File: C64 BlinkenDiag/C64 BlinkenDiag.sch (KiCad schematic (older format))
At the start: 14 parts, among them J1 C64-Exp-Port, J2 Voltmeter, M1 Mounting, M2 Mounting, M3 Mounting, M4 Mounting, SW1 ROM_EN, SW2 Function, SW3 Bank, SW4 Reset, U1 28C256

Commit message: Did a layout
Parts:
- added C1, C2, C3, C4, C5: 100nF, Capacitor_THT:C_Disc_D4.7mm_W2.5mm_P5.00mm, symbol Device:C_Small
- added C6: 10uF, Capacitor_THT:CP_Radial_D4.0mm_P2.00mm, symbol Device:CP_Small
- added D1: RESET, LED_THT:LED_D5.0mm, symbol Device:LED_Small
- added D10: D6, LED_THT:LED_D5.0mm, symbol Device:LED_Small
- added D11: D5, LED_THT:LED_D5.0mm, symbol Device:LED_Small
- added D12: D4, LED_THT:LED_D5.0mm, symbol Device:LED_Small
- added D13: D3, LED_THT:LED_D5.0mm, symbol Device:LED_Small
- added D14: D2, LED_THT:LED_D5.0mm, symbol Device:LED_Small
- added D15: D1, LED_THT:LED_D5.0mm, symbol Device:LED_Small
- added D16: D0, LED_THT:LED_D5.0mm, symbol Device:LED_Small
- added D17: A15, LED_THT:LED_D5.0mm, symbol Device:LED_Small
- added D18: A14, LED_THT:LED_D5.0mm, symbol Device:LED_Small
- added D19: A13, LED_THT:LED_D5.0mm, symbol Device:LED_Small
- added D2: GAME, LED_THT:LED_D5.0mm, symbol Device:LED_Small
- added D20: A12, LED_THT:LED_D5.0mm, symbol Device:LED_Small
- added D21: A11, LED_THT:LED_D5.0mm, symbol Device:LED_Small
- added D22: A10, LED_THT:LED_D5.0mm, symbol Device:LED_Small
- added D23: A9, LED_THT:LED_D5.0mm, symbol Device:LED_Small
- added D24: A8, LED_THT:LED_D5.0mm, symbol Device:LED_Small
- added D25: A7, LED_THT:LED_D5.0mm, symbol Device:LED_Small
- added D26: A6, LED_THT:LED_D5.0mm, symbol Device:LED_Small
- added D27: A5, LED_THT:LED_D5.0mm, symbol Device:LED_Small
- added D28: A4, LED_THT:LED_D5.0mm, symbol Device:LED_Small
- added D29: A3, LED_THT:LED_D5.0mm, symbol Device:LED_Small
- added D3: EXROM, LED_THT:LED_D5.0mm, symbol Device:LED_Small
- added D30: A2, LED_THT:LED_D5.0mm, symbol Device:LED_Small
- added D31: A1, LED_THT:LED_D5.0mm, symbol Device:LED_Small
- added D32: A0, LED_THT:LED_D5.0mm, symbol Device:LED_Small
- added D4: IO2, LED_THT:LED_D5.0mm, symbol Device:LED_Small
- added D5: IO1, LED_THT:LED_D5.0mm, symbol Device:LED_Small
- added D6: WRITE, LED_THT:LED_D5.0mm, symbol Device:LED_Small
- added D7: IRQ, LED_THT:LED_D5.0mm, symbol Device:LED_Small
- added D8: NMI, LED_THT:LED_D5.0mm, symbol Device:LED_Small
- added D9: D7, LED_THT:LED_D5.0mm, symbol Device:LED_Small
- added JP1: EN_SIGNAL, Connector_PinHeader_2.54mm:PinHeader_1x03_P2.54mm_Vertical, symbol Jumper:Jumper_3_Bridged12
- added JP2: EN_DATA, Connector_PinHeader_2.54mm:PinHeader_1x03_P2.54mm_Vertical, symbol Jumper:Jumper_3_Bridged12
- added JP3, JP4: EN_ADDR, Connector_PinHeader_2.54mm:PinHeader_1x03_P2.54mm_Vertical, symbol Jumper:Jumper_3_Bridged12
- added RN1, RN2, RN3, RN4: 330x8, Resistor_THT:R_Array_SIP9, symbol Device:R_Network08
- added U2: 74HCT540, Package_DIP:DIP-20_W7.62mm_Socket_LongPads, symbol 74xx:74LS540
- added U3, U4, U5: 74HCT573, Package_DIP:DIP-20_W7.62mm_Socket_LongPads, symbol 74xx:74LS573
- A1: footprint (none) -> voltmeter:voltage_display_036
- M1, M2, M3, M4: footprint mounting:M3 -> mounting:M3_pin
- SW2: value Function -> FUNCTION
- SW3: value Bank -> ROM_BANK
- SW4: value Reset -> RESET
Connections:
- net A0: now also U5.9 (D7)
- net A1: now also U5.8 (D6)
- net A10: now also U4.7 (D5)
- net A11: now also U4.6 (D4)
- net A12: now also U4.5 (D3)
- net A13: now also J1.J (A13), U4.4 (D2); no longer R1.2, SW1.4 (A), SW2.1 (A), U1.26 (A13)
- net A14: now also J1.H (A14), U4.3 (D1); no longer R2.2, SW3.1 (A), U1.1 (A14)
- net A2: now also U5.7 (D5)
- net A3: now also U5.6 (D4)
- net A4: now also U5.5 (D3)
- net A5: now also U5.4 (D2)
- net A6: now also U5.3 (D1)
- net A7: now also U5.2 (D0)
- net A8: now also U4.9 (D7)
- net A9: now also U4.8 (D6)
- net D0: now also U3.9 (D7)
- net D1: now also U3.8 (D6)
- net D2: now also U3.7 (D5)
- net D3: now also U3.6 (D4)
- net D4: now also U3.5 (D3)
- net D5: now also U3.4 (D2)
- net D6: now also U3.3 (D1)
- net D7: now also U3.2 (D0)
- net GND: now also C1.2, C2.2, C3.2, C4.2, C5.2, C6.2, JP1.1 (A), JP2.1 (A), JP3.1 (A), JP4.1 (A), RN1.1 (common), RN2.1 (common), RN3.1 (common), RN4.1 (common), U2.10 (GND), U3.10 (GND), U4.10 (GND), U5.10 (GND)
- net VCC: now also C1.1, C2.1, C3.1, C4.1, C5.1, C6.1, JP1.3 (B), JP2.3 (B), JP3.3 (B), JP4.3 (B), U2.20 (VCC), U3.20 (VCC), U4.20 (VCC), U5.20 (VCC)
- net ~EXROM: now also U2.4 (A2)
- net ~GAME: now also U2.3 (A1)
- net ~RESET: now also U2.2 (A0)
- net ~IO2: now reaches J1.10 (~IO2)
- net ~IO2: now also U2.5 (A3)
- net ~IRQ: now reaches J1.4 (~IRQ)
- net ~IRQ: now also U2.8 (A6)
- net R~W: now reaches J1.5 (R/~W)
- net R~W: now also U2.7 (A5)
- net ~IO1: now reaches J1.7 (~IO1)
- net ~IO1: now also U2.6 (A4)
- net ~NMI: now reaches J1.D (~NMI)
- net ~NMI: now also U2.9 (A7)
- net PHI2: now reaches J1.E (PHI2)
- net PHI2: now also U3.11 (Load), U4.11 (Load), U5.11 (Load)
- net A15: now reaches J1.F (A15)
- net A15: now also U4.2 (D0)
- net ~ROM renamed ~ROM_CS
- new net: JP1.2 (C), U2.1 (G1), U2.19 (G2)
- new net: D8.2 (A), U2.11 (Y7)
- new net: D7.2 (A), U2.12 (Y6)
- new net: D6.2 (A), U2.13 (Y5)
- new net: D5.2 (A), U2.14 (Y4)
- new net: D4.2 (A), U2.15 (Y3)
- new net: D3.2 (A), U2.16 (Y2)
- new net: D2.2 (A), U2.17 (Y1)
- new net: D1.2 (A), U2.18 (Y0)
- new net: D1.1 (K), RN2.2 (R1)
- new net: D2.1 (K), RN2.3 (R2)
- new net: D3.1 (K), RN2.4 (R3)
- new net: D4.1 (K), RN2.5 (R4)
- new net: D5.1 (K), RN2.6 (R5)
- new net: D6.1 (K), RN2.7 (R6)
- new net: D7.1 (K), RN2.8 (R7)
- new net: D8.1 (K), RN2.9 (R8)
- new net: JP2.2 (C), U3.1 (OE)
- new net: D16.2 (A), U3.12 (Q7)
- new net: D15.2 (A), U3.13 (Q6)
- new net: D14.2 (A), U3.14 (Q5)
- new net: D13.2 (A), U3.15 (Q4)
- new net: D12.2 (A), U3.16 (Q3)
- new net: D11.2 (A), U3.17 (Q2)
- new net: D10.2 (A), U3.18 (Q1)
- new net: D9.2 (A), U3.19 (Q0)
- new net: D9.1 (K), RN1.2 (R1)
- new net: D10.1 (K), RN1.3 (R2)
- new net: D11.1 (K), RN1.4 (R3)
- new net: D12.1 (K), RN1.5 (R4)
- new net: D13.1 (K), RN1.6 (R5)
- new net: D14.1 (K), RN1.7 (R6)
- new net: D15.1 (K), RN1.8 (R7)
- new net: D16.1 (K), RN1.9 (R8)
- new net: JP4.2 (C), U5.1 (OE)
- new net: D32.2 (A), U5.12 (Q7)
- new net: D31.2 (A), U5.13 (Q6)
- new net: D30.2 (A), U5.14 (Q5)
- new net: D29.2 (A), U5.15 (Q4)
- new net: D28.2 (A), U5.16 (Q3)
- new net: D27.2 (A), U5.17 (Q2)
- new net: D26.2 (A), U5.18 (Q1)
- new net: D25.2 (A), U5.19 (Q0)
- new net: D25.1 (K), RN4.2 (R1)
- new net: D26.1 (K), RN4.3 (R2)
- new net: D27.1 (K), RN4.4 (R3)
- new net: D28.1 (K), RN4.5 (R4)
- new net: D29.1 (K), RN4.6 (R5)
- new net: D30.1 (K), RN4.7 (R6)
- new net: D31.1 (K), RN4.8 (R7)
- new net: D32.1 (K), RN4.9 (R8)
- new net: JP3.2 (C), U4.1 (OE)
- new net: D24.2 (A), U4.12 (Q7)
- new net: D23.2 (A), U4.13 (Q6)
- new net: D22.2 (A), U4.14 (Q5)
- new net: D21.2 (A), U4.15 (Q4)
- new net: D20.2 (A), U4.16 (Q3)
- new net: D19.2 (A), U4.17 (Q2)
- new net: D18.2 (A), U4.18 (Q1)
- new net: D17.2 (A), U4.19 (Q0)
- new net: D17.1 (K), RN3.2 (R1)
- new net: D18.1 (K), RN3.3 (R2)
- new net: D19.1 (K), RN3.4 (R3)
- new net: D20.1 (K), RN3.5 (R4)
- new net: D21.1 (K), RN3.6 (R5)
- new net: D22.1 (K), RN3.7 (R6)
- new net: D23.1 (K), RN3.8 (R7)
- new net: D24.1 (K), RN3.9 (R8)
- new net ROM_A13: R1.2, SW1.4 (A), SW2.1 (A), U1.26 (A13)
- new net ROM_A14: R2.2, SW3.1 (A), U1.1 (A14)
- no-connect marks 18 -> 9
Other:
- moved on the sheet: A1, J2, R1, R2, SW1A, SW1B, SW2A, SW2B, SW3A, SW3B

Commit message: Tweaked silkscreen and gerber export
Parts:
- J2: value Voltmeter -> VOLTMETER
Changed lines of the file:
@@
 Wire Wire Line
 	7925 1850 8200 1850
-Wire Bus Line
-	5750 2250 5750 4350
-Wire Bus Line
-	3500 1850 3500 4350
-Wire Bus Line
-	925  1850 925  4350
-Wire Bus Line
-	5875 2250 5875 6025
-Wire Bus Line
-	8825 1950 8825 6025
 $Comp
 L 74xx:74LS540 U2
@@
 P 7675 1050
 F 0 "J2" H 7592 1315 50  0000 C CNN
-F 1 "Voltmeter" H 7592 1224 50  0000 C CNN
+F 1 "VOLTMETER" H 7592 1224 50  0000 C CNN
 F 2 "Connector_JST:JST_XH_B2B-XH-A_1x02_P2.50mm_Vertical" H 7625 1200 50  0001 C CNN
 F 3 "~" H 7625 1200 50  0001 C CNN
@@
 	-1   0    0    -1
 $EndComp
+Wire Bus Line
+	5750 2250 5750 4350
+Wire Bus Line
+	3500 1850 3500 4350
+Wire Bus Line
+	925  1850 925  4350
+Wire Bus Line
+	5875 2250 5875 6025
+Wire Bus Line
+	8825 1950 8825 6025
 $EndSCHEMATC

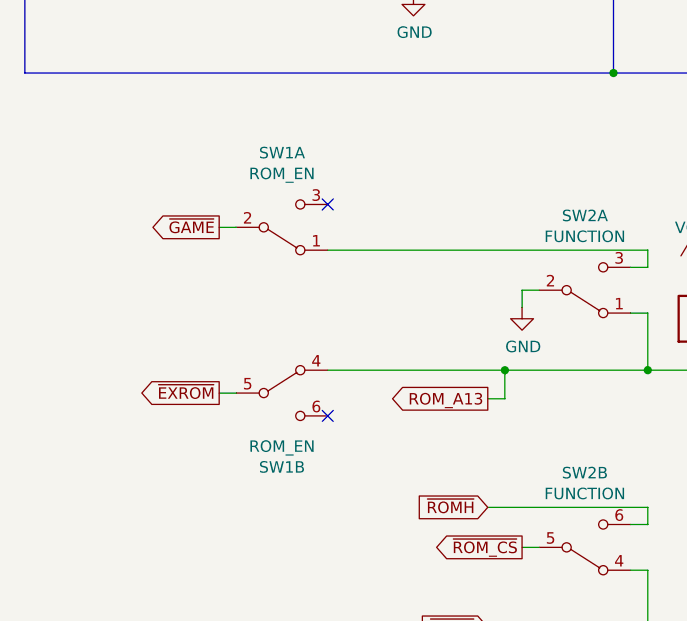
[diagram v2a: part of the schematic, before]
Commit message: Added faceplate and changed ROM_EN to ROM_DIS
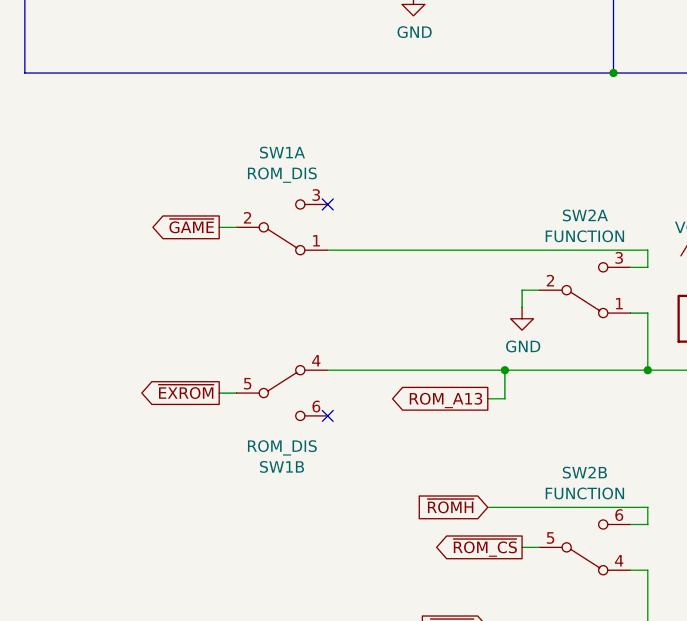
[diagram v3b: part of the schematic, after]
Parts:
- SW1: value ROM_EN -> ROM_DIS
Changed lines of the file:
@@
 P 2050 5025
 F 0 "SW1" H 2050 4700 50  0000 C CNN
-F 1 "ROM_EN" H 2050 4791 50  0000 C CNN
+F 1 "ROM_DIS" H 2050 4791 50  0000 C CNN
 F 2 "6pin_switch:dpdt_switch_black" H 2050 5025 50  0001 C CNN
 F 3 "~" H 2050 5025 50  0001 C CNN
@@
 P 2050 5750
 F 0 "SW1" H 2050 5425 50  0000 C CNN
-F 1 "ROM_EN" H 2050 5516 50  0000 C CNN
+F 1 "ROM_DIS" H 2050 5516 50  0000 C CNN
 F 2 "6pin_switch:dpdt_switch_black" H 2050 5750 50  0001 C CNN
 F 3 "~" H 2050 5750 50  0001 C CNN
